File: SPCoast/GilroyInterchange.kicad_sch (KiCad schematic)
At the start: 72 parts, among them SW5777 777, SW5781 781

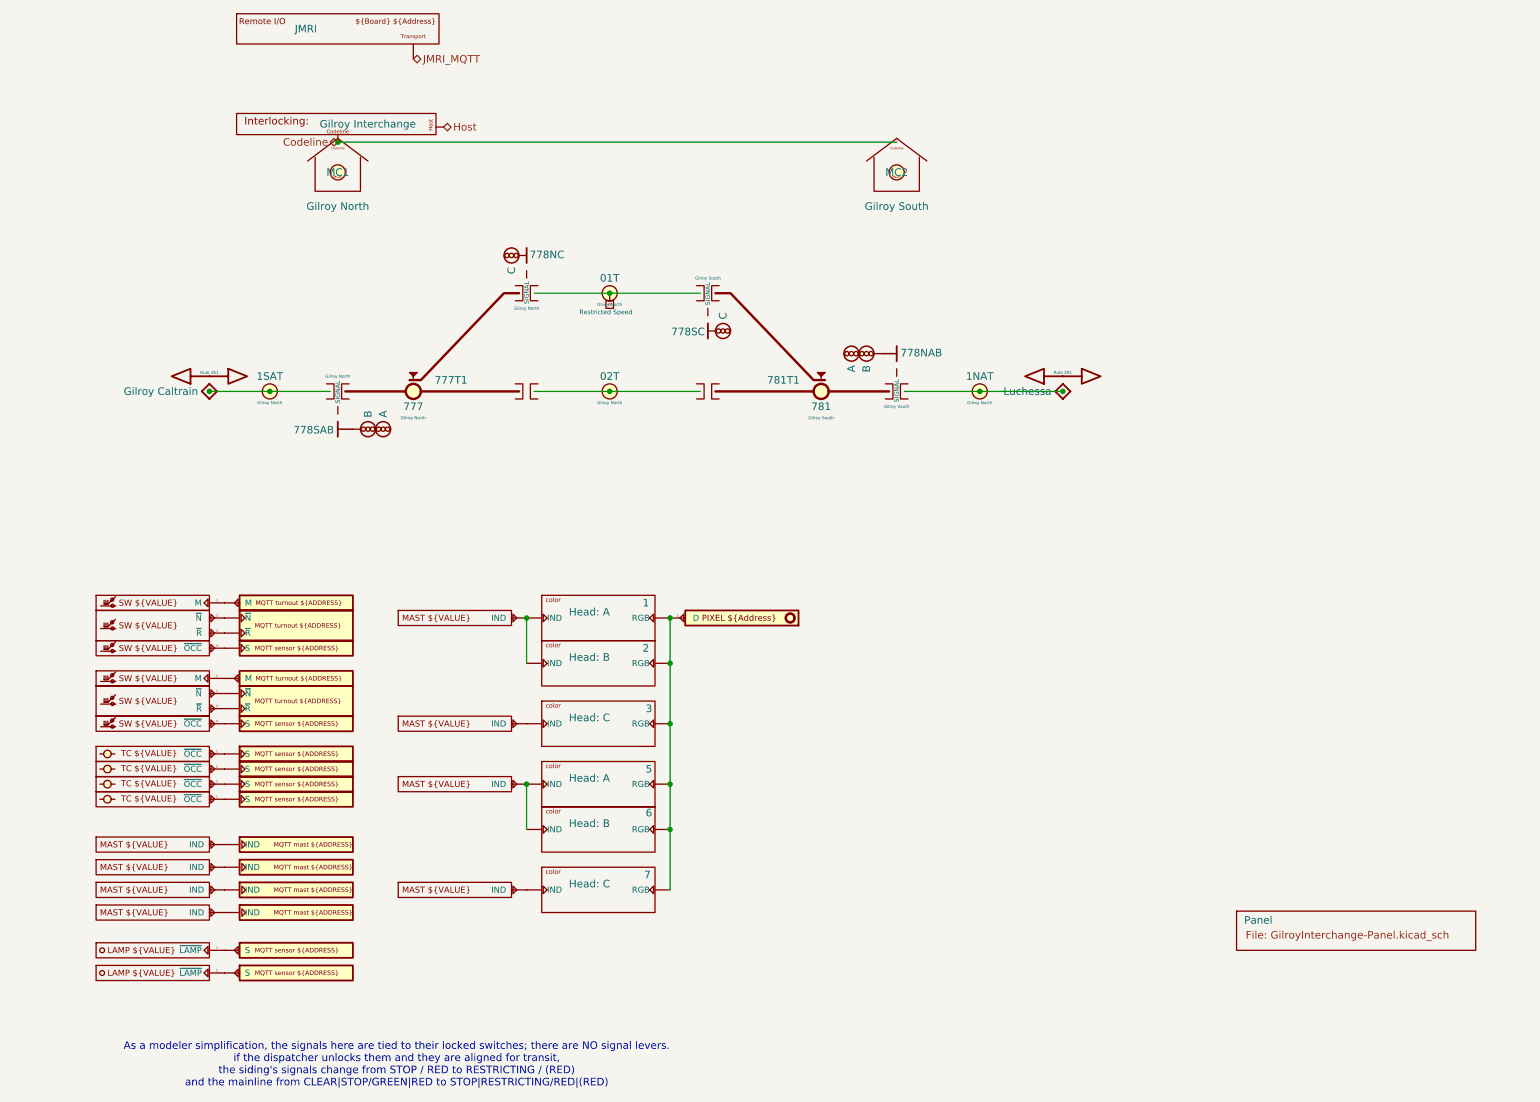
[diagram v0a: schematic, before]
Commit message: chore(kicad): owner edits: uniform unit ports Codeline, Host, IOBus, OfficeIOBus; panels on the desk bus
Owner's edits, committed as they stand (2026-10-21): every unit sheet exposes the same four
ports and the parent wires only the ones it needs; Caltrain's and Interchange's panels reach
the desk bus through OfficeIOBus; unused ports carry no-connect flags; grid snaps fixed.
Two label spellings are still mismatched (Luchessa's OfficeIOBus vs the root's OfficeBusIO;
Interchange's JMRI_MQTT vs the root's IOBus), fixed in the next commit.
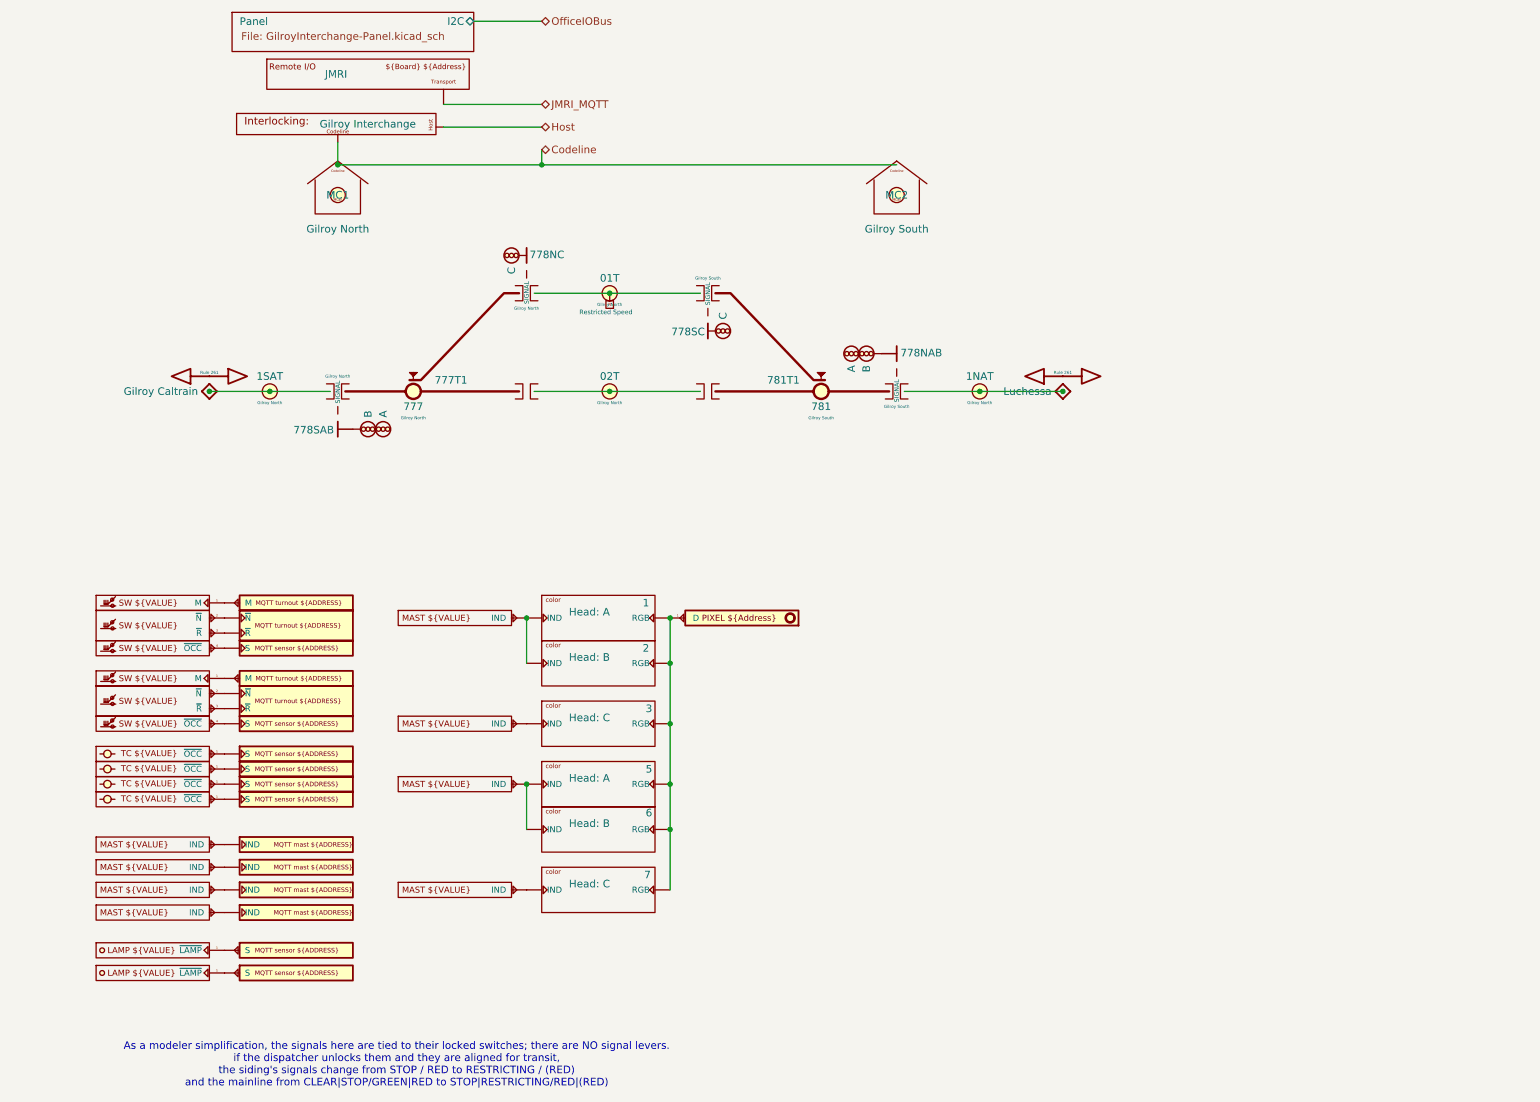
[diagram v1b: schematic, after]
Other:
- sheet Panel ports: added I2C; removed none
